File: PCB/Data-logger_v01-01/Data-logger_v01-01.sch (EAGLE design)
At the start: 33 parts, among them J1 6364372-1, Q4 LF33CV, U2 LPC1549JBD48, X1 22-23-2081, X2 22-23-2021, X3 87758-0416

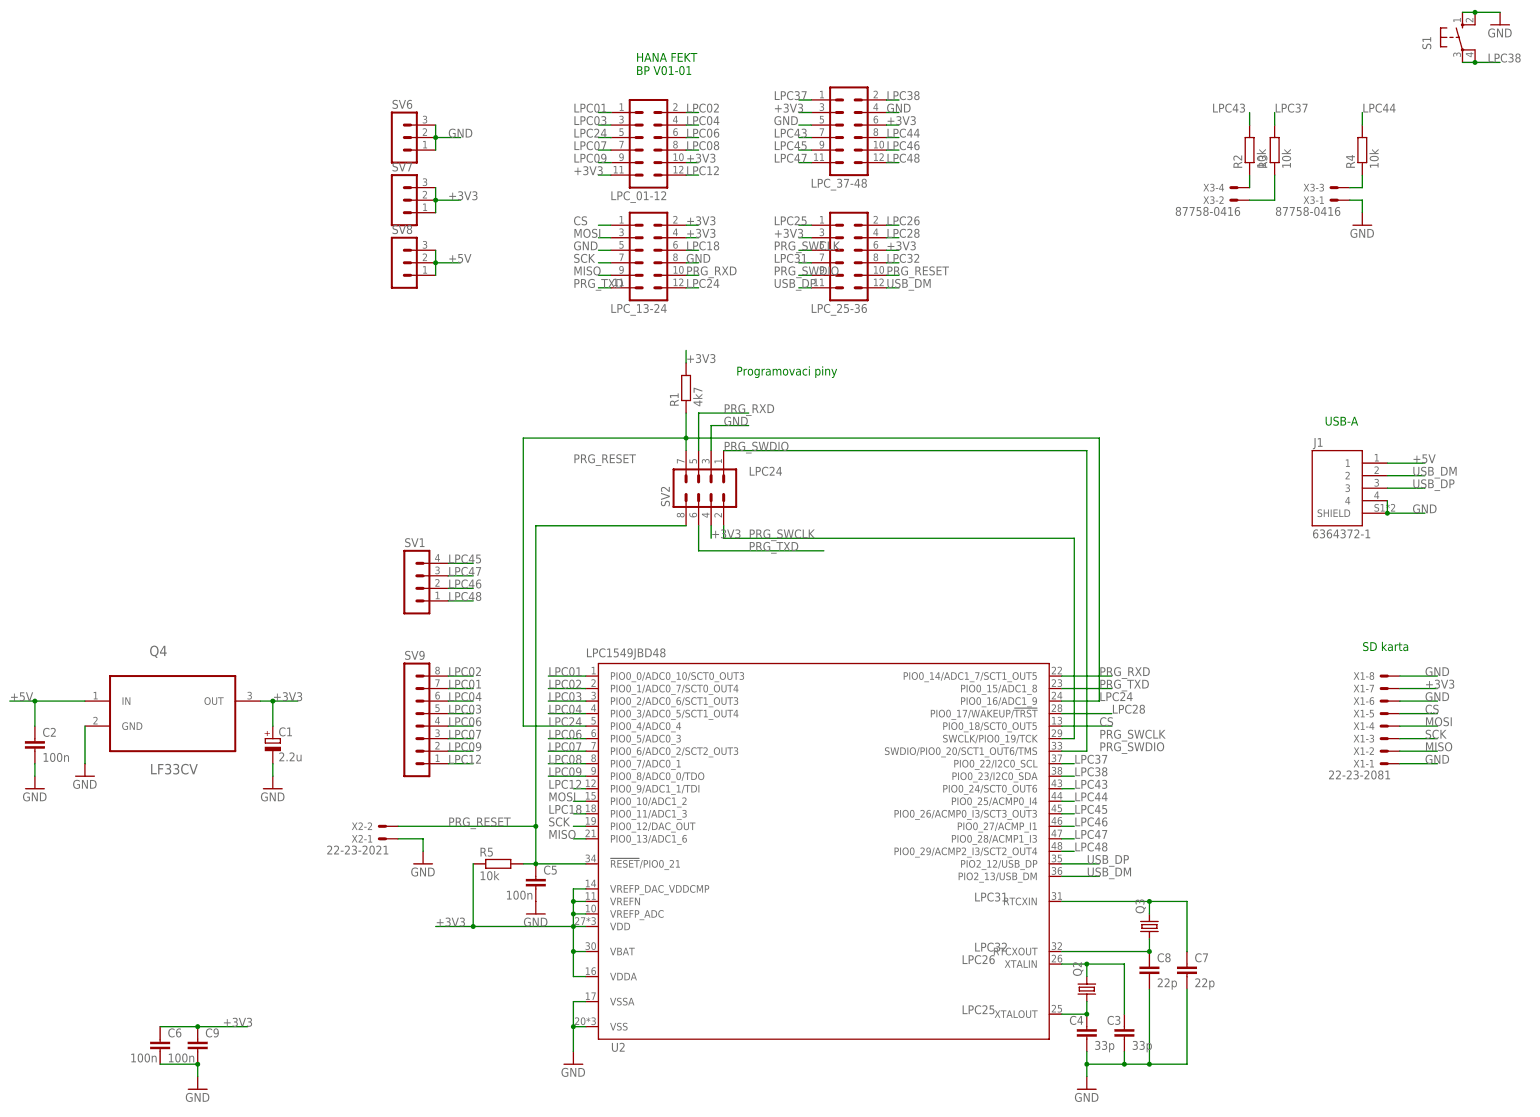
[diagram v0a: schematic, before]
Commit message: update components values
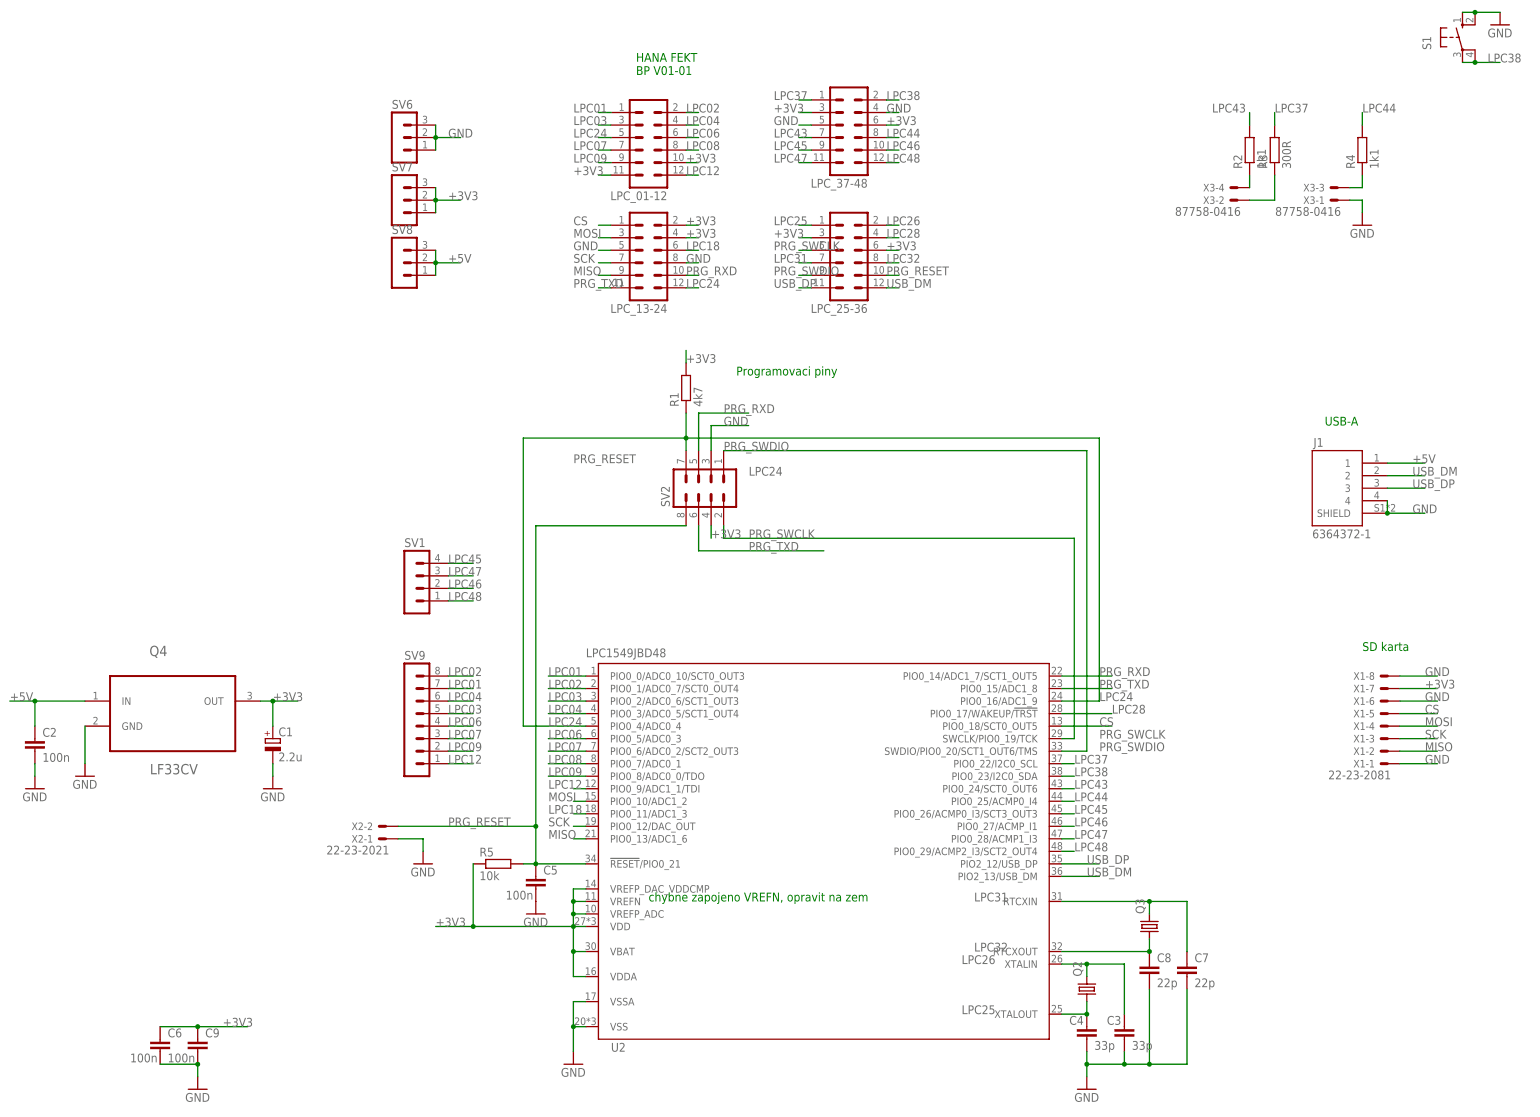
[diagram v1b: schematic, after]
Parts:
- R2, R4: value 10k -> 1k1
- R3: value 10k -> 300R
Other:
- note added: "chybne zapojeno VREFN, opravit na zem"
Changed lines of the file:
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@@
 <grid distance="0.1" unitdist="inch" unit="inch" style="lines" multiple="1" display="no" altdistance="0.01" altunitdist="inch" altunit="inch"/>
 <layers>
-<layer number="1" name="Top" color="4" fill="1" visible="yes" active="no"/>
-<layer number="16" name="Bottom" color="1" fill="1" visible="yes" active="no"/>
-<layer number="17" name="Pads" color="2" fill="1" visible="yes" active="no"/>
-<layer number="18" name="Vias" color="2" fill="1" visible="yes" active="no"/>
-<layer number="19" name="Unrouted" color="6" fill="1" visible="yes" active="no"/>
-<layer number="20" name="Dimension" color="24" fill="1" visible="yes" active="no"/>
-<layer number="21" name="tPlace" color="7" fill="1" visible="yes" active="no"/>
-<layer number="22" name="bPlace" color="7" fill="1" visible="yes" active="no"/>
-<layer number="23" name="tOrigins" color="15" fill="1" visible="yes" active="no"/>
-<layer number="24" name="bOrigins" color="15" fill="1" visible="yes" active="no"/>
-<layer number="25" name="tNames" color="7" fill="1" visible="yes" active="no"/>
-<layer number="26" name="bNames" color="7" fill="1" visible="yes" active="no"/>
-<layer number="27" name="tValues" color="7" fill="1" visible="yes" active="no"/>
-<layer number="28" name="bValues" color="7" fill="1" visible="yes" active="no"/>
+<layer number="1" name="Top" color="4" fill="1" visible="no" active="no"/>
+<layer number="16" name="Bottom" color="1" fill="1" visible="no" active="no"/>
+<layer number="17" name="Pads" color="2" fill="1" visible="no" active="no"/>
+<layer number="18" name="Vias" color="2" fill="1" visible="no" active="no"/>
+<layer number="19" name="Unrouted" color="6" fill="1" visible="no" active="no"/>
+<layer number="20" name="Dimension" color="24" fill="1" visible="no" active="no"/>
+<layer number="21" name="tPlace" color="7" fill="1" visible="no" active="no"/>
+<layer number="22" name="bPlace" color="7" fill="1" visible="no" active="no"/>
+<layer number="23" name="tOrigins" color="15" fill="1" visible="no" active="no"/>
+<layer number="24" name="bOrigins" color="15" fill="1" visible="no" active="no"/>
+<layer number="25" name="tNames" color="7" fill="1" visible="no" active="no"/>
+<layer number="26" name="bNames" color="7" fill="1" visible="no" active="no"/>
+<layer number="27" name="tValues" color="7" fill="1" visible="no" active="no"/>
+<layer number="28" name="bValues" color="7" fill="1" visible="no" active="no"/>
 <layer number="29" name="tStop" color="7" fill="3" visible="no" active="no"/>
 <layer number="30" name="bStop" color="7" fill="6" visible="no" active="no"/>
@@
 <layer number="35" name="tGlue" color="7" fill="4" visible="no" active="no"/>
 <layer number="36" name="bGlue" color="7" fill="5" visible="no" active="no"/>
-<layer number="37" name="tTest" color="7" fill="1" visible="yes" active="no"/>
-<layer number="38" name="bTest" color="7" fill="1" visible="yes" active="no"/>
+<layer number="37" name="tTest" color="7" fill="1" visible="no" active="no"/>
+<layer number="38" name="bTest" color="7" fill="1" visible="no" active="no"/>
 <layer number="39" name="tKeepout" color="4" fill="11" visible="no" active="no"/>
 <layer number="40" name="bKeepout" color="1" fill="11" visible="no" active="no"/>
@@
 <layer number="44" name="Drills" color="7" fill="1" visible="no" active="no"/>
 <layer number="45" name="Holes" color="7" fill="1" visible="no" active="no"/>
-<layer number="46" name="Milling" color="3" fill="1" visible="yes" active="no"/>
-<layer number="47" name="Measures" color="7" fill="1" visible="yes" active="no"/>
-<layer number="48" name="Document" color="7" fill="1" visible="yes" active="no"/>
-<layer number="49" name="Reference" color="7" fill="1" visible="yes" active="no"/>
-<layer number="51" name="tDocu" color="7" fill="1" visible="yes" active="no"/>
-<layer number="52" name="bDocu" color="7" fill="1" visible="yes" active="no"/>
+<layer number="46" name="Milling" color="3" fill="1" visible="no" active="no"/>
+<layer number="47" name="Measures" color="7" fill="1" visible="no" active="no"/>
+<layer number="48" name="Document" color="7" fill="1" visible="no" active="no"/>
+<layer number="49" name="Reference" color="7" fill="1" visible="no" active="no"/>
+<layer number="51" name="tDocu" color="7" fill="1" visible="no" active="no"/>
+<layer number="52" name="bDocu" color="7" fill="1" visible="no" active="no"/>
 <layer number="88" name="SimResults" color="9" fill="1" visible="yes" active="yes"/>
 <layer number="89" name="SimProbes" color="9" fill="1" visible="yes" active="yes"/>
@@
 <part name="S1" library="switch-omron" library_urn="urn:adsk.eagle:library:377" deviceset="10-XX" device="" package3d_urn="urn:adsk.eagle:package:27496/1"/>
 <part name="X3" library="con-molex" deviceset="87758-0416" device="" package3d_urn="urn:adsk.eagle:package:8078893/1"/>
-<part name="R2" library="rcl" library_urn="urn:adsk.eagle:library:334" deviceset="R-EU_" device="R1206W" package3d_urn="urn:adsk.eagle:package:23539/2" value="10k"/>
-<part name="R3" library="rcl" library_urn="urn:adsk.eagle:library:334" deviceset="R-EU_" device="R1206W" package3d_urn="urn:adsk.eagle:package:23539/2" value="10k"/>
-<part name="R4" library="rcl" library_urn="urn:adsk.eagle:library:334" deviceset="R-EU_" device="R1206W" package3d_urn="urn:adsk.eagle:package:23539/2" value="10k"/>
+<part name="R2" library="rcl" library_urn="urn:adsk.eagle:library:334" deviceset="R-EU_" device="R1206W" package3d_urn="urn:adsk.eagle:package:23539/2" value="1k1"/>
+<part name="R3" library="rcl" library_urn="urn:adsk.eagle:library:334" deviceset="R-EU_" device="R1206W" package3d_urn="urn:adsk.eagle:package:23539/2" value="300R"/>
+<part name="R4" library="rcl" library_urn="urn:adsk.eagle:library:334" deviceset="R-EU_" device="R1206W" package3d_urn="urn:adsk.eagle:package:23539/2" value="1k1"/>
 <part name="GND2" library="supply1" library_urn="urn:adsk.eagle:library:371" deviceset="GND" device=""/>
 <part name="GND3" library="supply1" library_urn="urn:adsk.eagle:library:371" deviceset="GND" device=""/>
@@
 <text x="101.6" y="86.36" size="1.778" layer="91">USB-A</text>
 <text x="-17.78" y="96.52" size="1.778" layer="91">Programovaci piny</text>
+<text x="-35.56" y="-10.16" size="1.778" layer="91">chybne zapojeno VREFN, opravit na zem</text>
 </plain>
 <instances>
